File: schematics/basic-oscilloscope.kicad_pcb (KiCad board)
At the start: 2 copper layers, 107.7 x 62.2 mm, 18 parts, among them J1 9V_BATTERY, J2 12V_DC_JACK, SW5 SW_SPST, U1 LT3032-3.3, U2 STM32F103C8Tx, U6 LM78L05_SO8

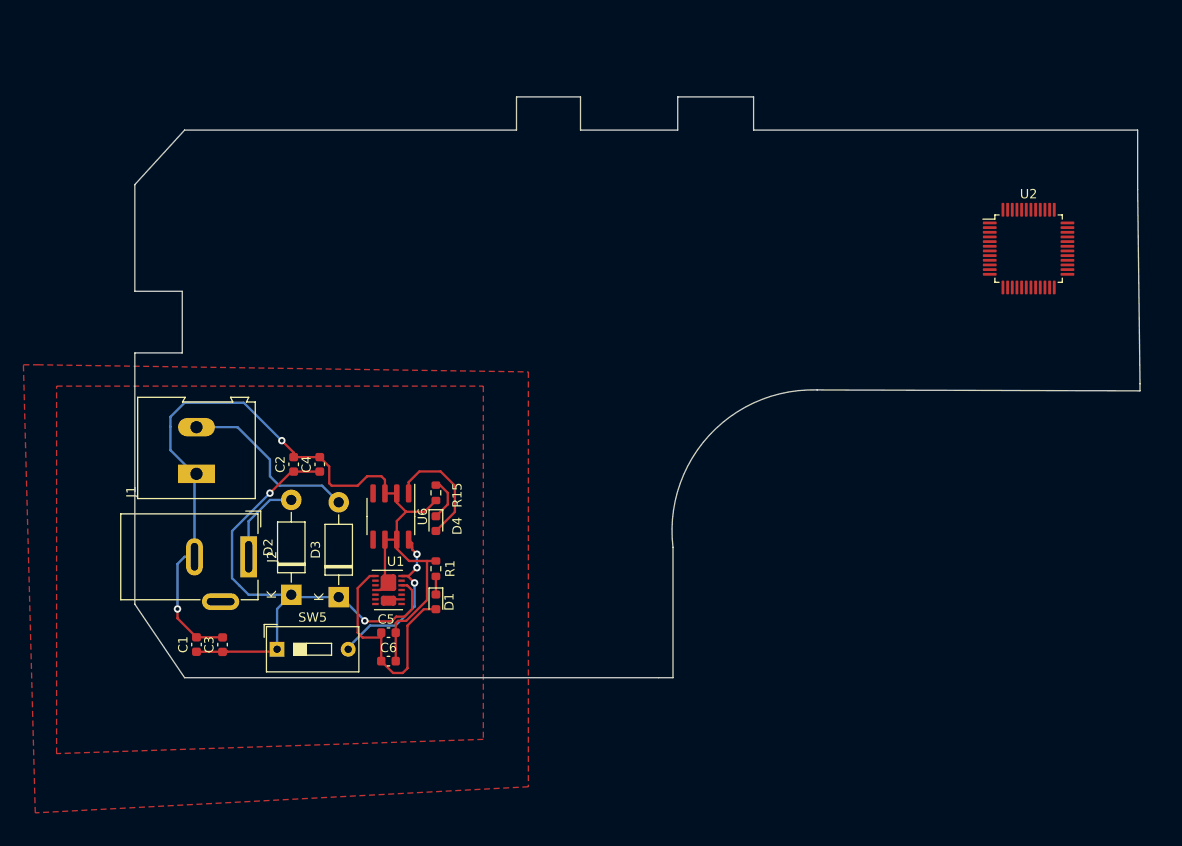
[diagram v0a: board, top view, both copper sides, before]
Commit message: update component footprints
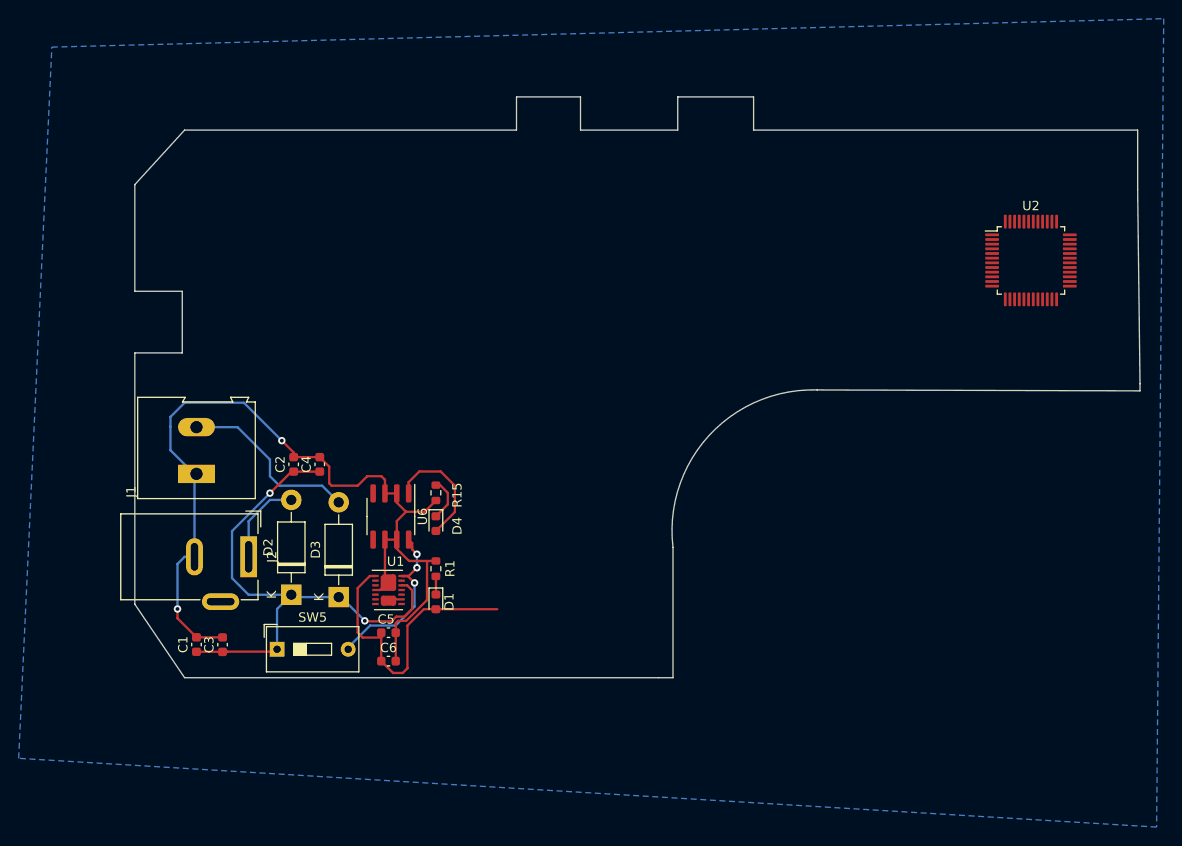
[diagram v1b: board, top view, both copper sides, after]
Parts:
- moved U2 1.30 mm to (194.6, 88.6)
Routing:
- net 3.3V: track 24.9 -> 31.5 mm
- added copper zone on B.Cu, net 0
- removed copper zone on F.Cu, net 0
